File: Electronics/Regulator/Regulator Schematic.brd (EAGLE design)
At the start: 38.1 x 38.1 mm, 18 parts

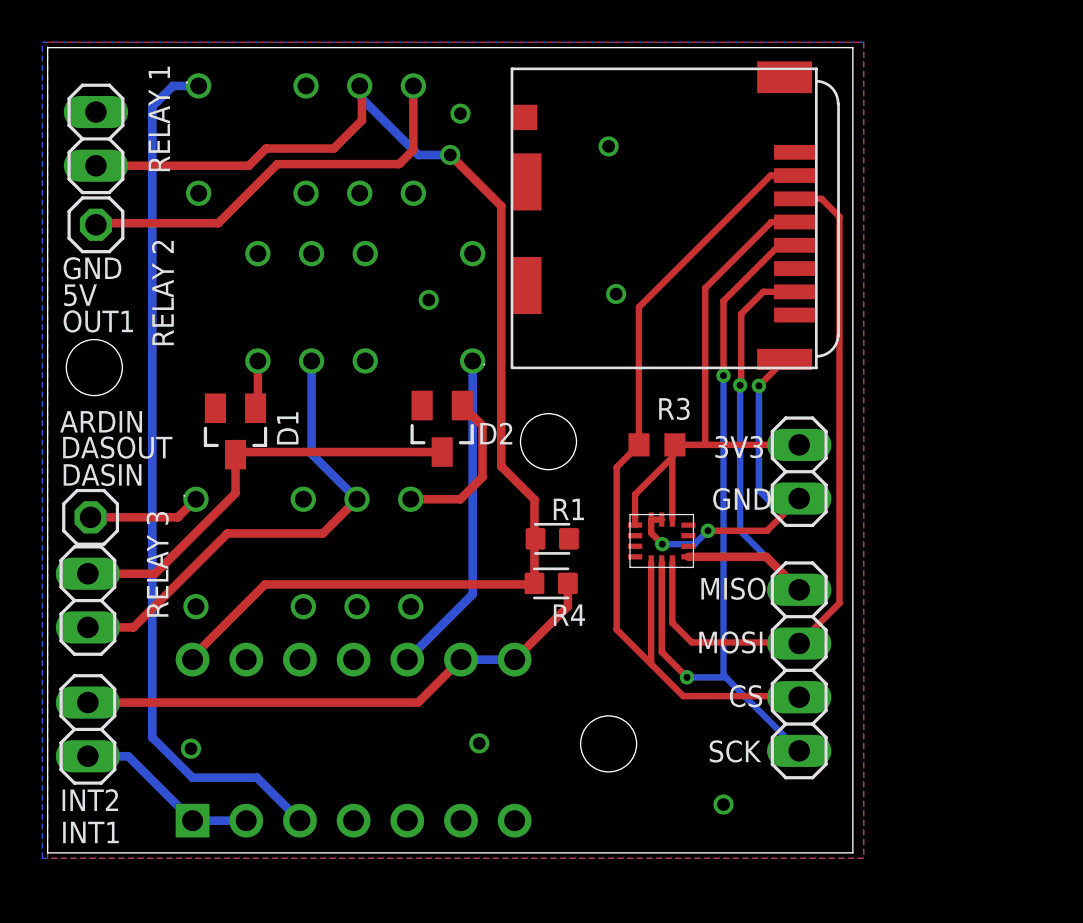
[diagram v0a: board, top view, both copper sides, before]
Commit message: rerouted relay board, also put the power regulator in this repo from last years
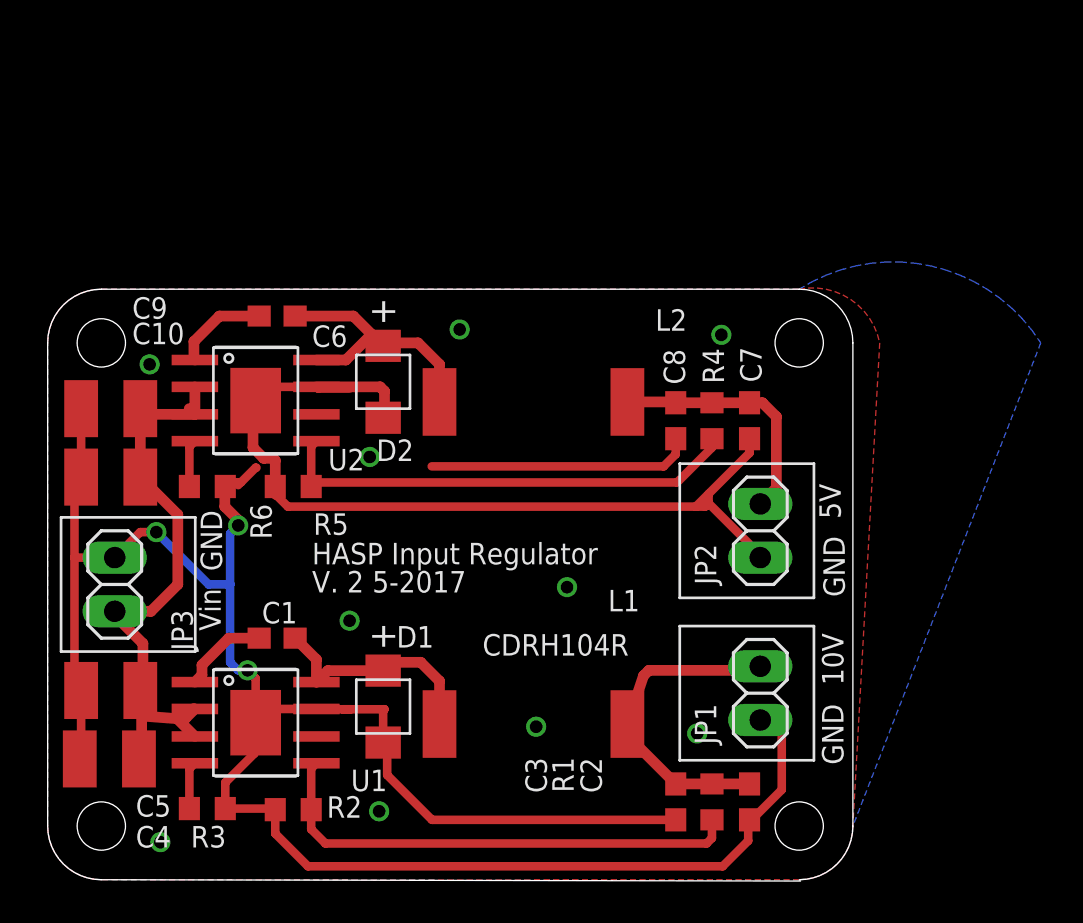
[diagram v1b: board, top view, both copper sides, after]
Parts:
- removed JP10: (no value), pinhead:1X01
- removed JP13, JP5: (no value), pinhead:1X02
- removed JP6: (no value), pinhead:1X04
- removed U$1: (no value), IMU:IMU
- removed U$2, U$3, U$8: (no value), relay board:EC2-5SNU
- removed U$4: MICRO_SD, NR_connectors:MICRO_SD_HINGED
- removed U$5: CD4093BE, NAND Gates:CD4093BE
- added C1, C6: .1 uF, resistor:C0603
- added C10, C5: 2.2 uF, resistor:C1210
- added C2, C7: .18 uF, resistor:C0603
- added C3, C8: 10 uF, resistor:C0603
- added C4, C9: 10 uF, resistor:C1210
- added L1, L2: CDRH104R, library:CDRH104R
- added R2, R5: 13.3k, resistor:R0603
- added R6: 23.3k, resistor:R0603
- added U1, U2: LMR16020, HASP:SO8
- D1, D2: value BAT54 -> DO-214AC; device BAT54:SOT23 -> HASP:DO-214AC
- JP3: device pinhead:1X01 -> pinhead:1X02
- R1: value 47k -> 165k; device CRGS0603J1K5:RESC1608X50N -> resistor:R0603
- R3: value 1M -> 23.3k
- R4: value 47k -> 75k; device CRGS0603J1K5:RESC1608X50N -> resistor:R0603
- moved JP1 40.9 mm to (33.7, 7.56)
- moved R3 27.4 mm to (7.56, 2.10)
- moved D1 14.8 mm to (15.9, 6.92), turned to 90 degrees
- moved R1 14.6 mm to (31.4, 2.41), turned to 90 degrees
- moved R4 10.8 mm to (31.4, 20.4), turned to 90 degrees
- moved D2 3.57 mm to (15.9, 22.3), turned to 90 degrees
- moved JP3 3.37 mm to (3.17, 12.7), turned to 270 degrees
- moved JP2 3.35 mm to (33.7, 15.2), turned to 90 degrees
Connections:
- removed net +3V3: JP2.1, R3.1, U$1.5, U$1.8, U$4.VDD
- removed net +5V: JP1.1, R1.2, R4.1, U$2.4, U$5.P$14
- removed net ARDIN: JP3.1, U$8.1
- removed net COIL1: U$2.1, U$5.P$3
- removed net COIL2: U$3.1, U$5.P$10
- removed net CS: JP6.3, R3.2, U$1.12, U$4.CD
- removed net DASIN: JP13.1, U$3.4, U$8.4
- removed net DASOUT: D1.3, D2.3, JP13.2
- removed net INT1: JP5.1, U$5.P$1, U$5.P$2
- removed net INT2: JP5.2, R4.2, U$5.P$8, U$5.P$9
- removed net MISO: JP6.1, U$1.1, U$4.DAT0
- removed net MOSI: JP6.2, U$1.14, U$4.CMD
- removed net OUT1: JP10.1, U$2.5
- removed net SCK: JP6.4, U$1.13, U$4.CLK
- new net IN: C10.1, C4.1, C5.1, C9.1, JP3.2, U1.P$2, U1.P$3, U2.P$2, U2.P$3
- new net N$1: R6.2, U2.P$4
- new net N$14: C7.1, C8.1, JP2.2, L2.P$2, R4.2
- new net N$6: C6.2, U2.P$1
- new net N$7: C6.1, D2.P$2, L2.P$1, U2.P$8
- new net N$8: R4.1, R5.2, U2.P$5
- new net N$9: C2.1, C3.1, JP1.2, L1.P$2, R1.2
- net GND: now also C10.2, C2.2, C3.2, C4.2, C5.2, C7.2, C8.2, C9.2, D1.P$1, D2.P$1, JP1.1, JP2.1, JP3.1, R2.1, R3.1, R5.1, R6.1, U1.P$7, U1.PAD, U2.P$7, U2.PAD; no longer JP1.2, JP2.2, U$1.6, U$1.7, U$2.12, U$3.12, U$4.CD1, U$4.GND1, U$4.GND2, U$4.GND3, U$4.GND4, U$5.P$7, U$8.12
- net N$2: now also R3.2, U1.P$4; no longer R1.1
- net N$3: now also C1.2, U1.P$1; no longer D1.1, U$3.5
- net N$4: now also C1.1, D1.P$2, L1.P$1, U1.P$8; no longer D2.1, U$8.5
- net N$5: now also R1.1, R2.2, U1.P$5; no longer U$4.VSS
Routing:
- net GND: track 18.1 -> 161.3 mm, vias 3 -> 12
- net +5V: track 60.8 -> 0.00 mm, vias 1 -> 0
- net COIL1: track 41.1 -> 0.00 mm
- net CS: track 40.4 -> 0.00 mm
- net SCK: track 35.0 -> 0.00 mm, vias 2 -> 0
- net MOSI: track 32.7 -> 0.00 mm
- net IN: track 0.00 -> 29.7 mm
- net +3V3: track 26.4 -> 0.00 mm
- net INT2: track 25.7 -> 0.00 mm
- net N$5: track 0.00 -> 23.4 mm
- net MISO: track 23.1 -> 0.00 mm, vias 1 -> 0
- net DASIN: track 22.7 -> 0.00 mm
- net N$8: track 0.00 -> 22.4 mm, vias 1 -> 0
- net DASOUT: track 20.2 -> 0.00 mm
- net OUT1: track 19.5 -> 0.00 mm
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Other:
- board size 38.1 x 38.1 mm -> 38.1 x 28 mm
- board text added: "10V"
- board text added: "HASP Input Regulator"
- board text added: "V. 2 5-2017"
- board text added: "Vin"
- board text removed: "3V3"
- board text removed: "7.2018"
- board text removed: "ARDIN"
- board text removed: "CS"
- board text removed: "DASIN"
- board text removed: "DASOUT"
- board text removed: "HASP Relay Board"
- board text removed: "INT1"
- board text removed: "INT2"
- board text removed: "MISO"
- board text removed: "MOSI"
- board text removed: "OUT1"
- board text removed: "RELAY 1"
- board text removed: "RELAY 2"
- board text removed: "RELAY 3"
- board text removed: "SCK"
- board text removed: "V. 2"
